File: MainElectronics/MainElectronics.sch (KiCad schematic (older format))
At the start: 37 parts, among them J1 NVIDIA_Jetson_NX_Dev_40pin_Co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, J2 NVIDIA_Jetson_NX_Dev_Button_C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, M1 Motor_DC, M2 Motor_DC, M3 Motor_DC, M4 Motor_DC, M5 Motor_DC, M6 Motor_DC, M7 Motor_DC, M8 Motor_DC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

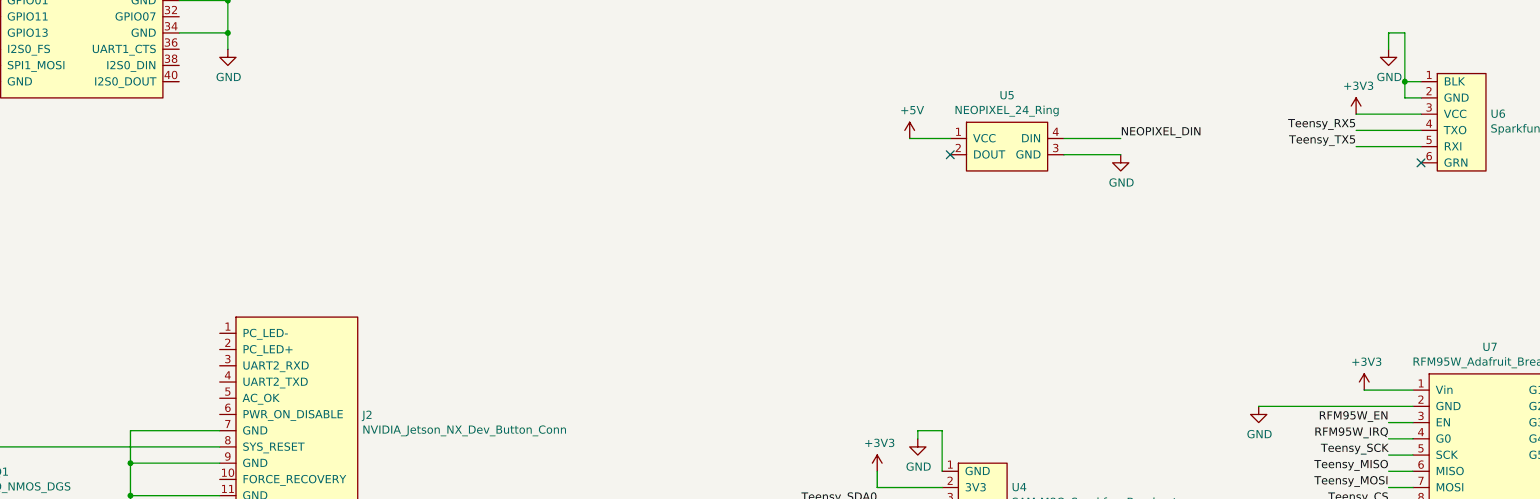
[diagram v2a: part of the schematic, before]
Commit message: Changed role of OpenLog after chat with software team
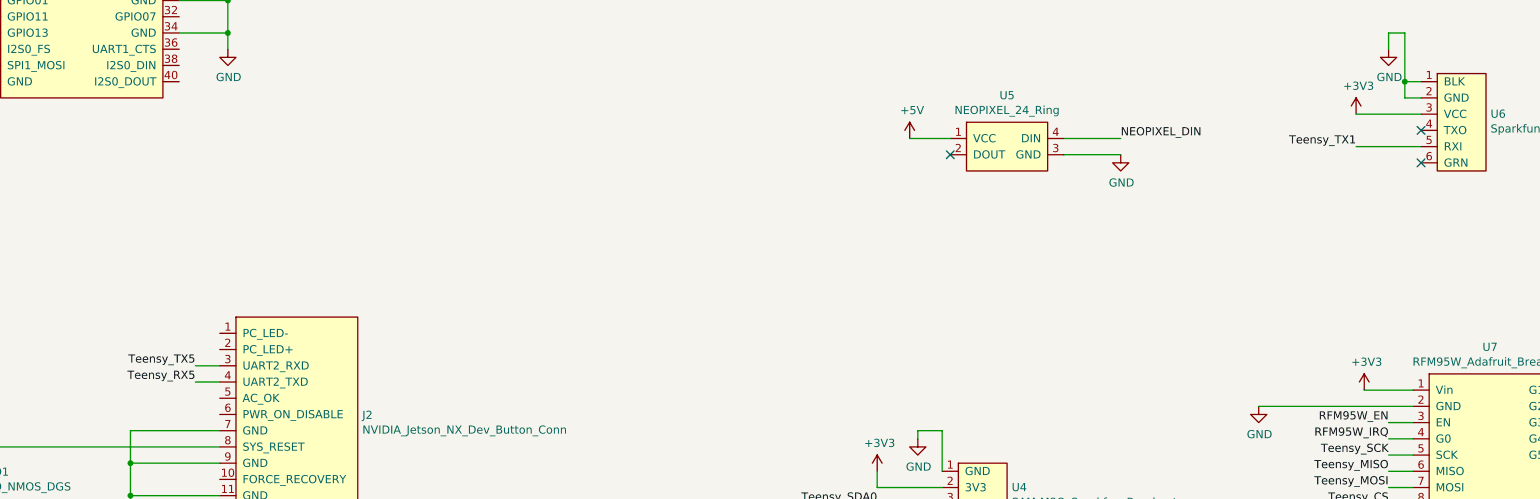
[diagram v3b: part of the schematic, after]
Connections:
- net Teensy_RX5: now also J2.4 (UART2_TXD); no longer U6.4 (TXO)
- net Teensy_TX1: now also U6.5 (RXI)
- net Teensy_TX5: now also J2.3 (UART2_RXD); no longer U6.5 (RXI)
- no-connect marks 29 -> 30
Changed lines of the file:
@@
 	7800 8400 6950 8400
 Wire Wire Line
-	11000 4150 10600 4150
-Wire Wire Line
 	11000 4250 10600 4250
-Text Label 10600 4150 2    50   ~ 0
-Teensy_RX5
-Text Label 10600 4250 2    50   ~ 0
-Teensy_TX5
 Text Label 3900 9550 0    50   ~ 0
 Teensy_RX5
@@
 	1    0    0    -1
 $EndComp
+Text Label 3450 5700 2    50   ~ 0
+Teensy_RX5
+Text Label 3450 5600 2    50   ~ 0
+Teensy_TX5
+Wire Wire Line
+	3450 5700 3600 5700
+Wire Wire Line
+	3450 5600 3600 5600
+Text Label 10600 4250 2    50   ~ 0
+Teensy_TX1
+NoConn ~ 11000 4150
 $EndSCHEMATC
